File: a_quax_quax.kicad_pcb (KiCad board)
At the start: 2 copper layers, 100.3 x 94.5 mm, 23 parts

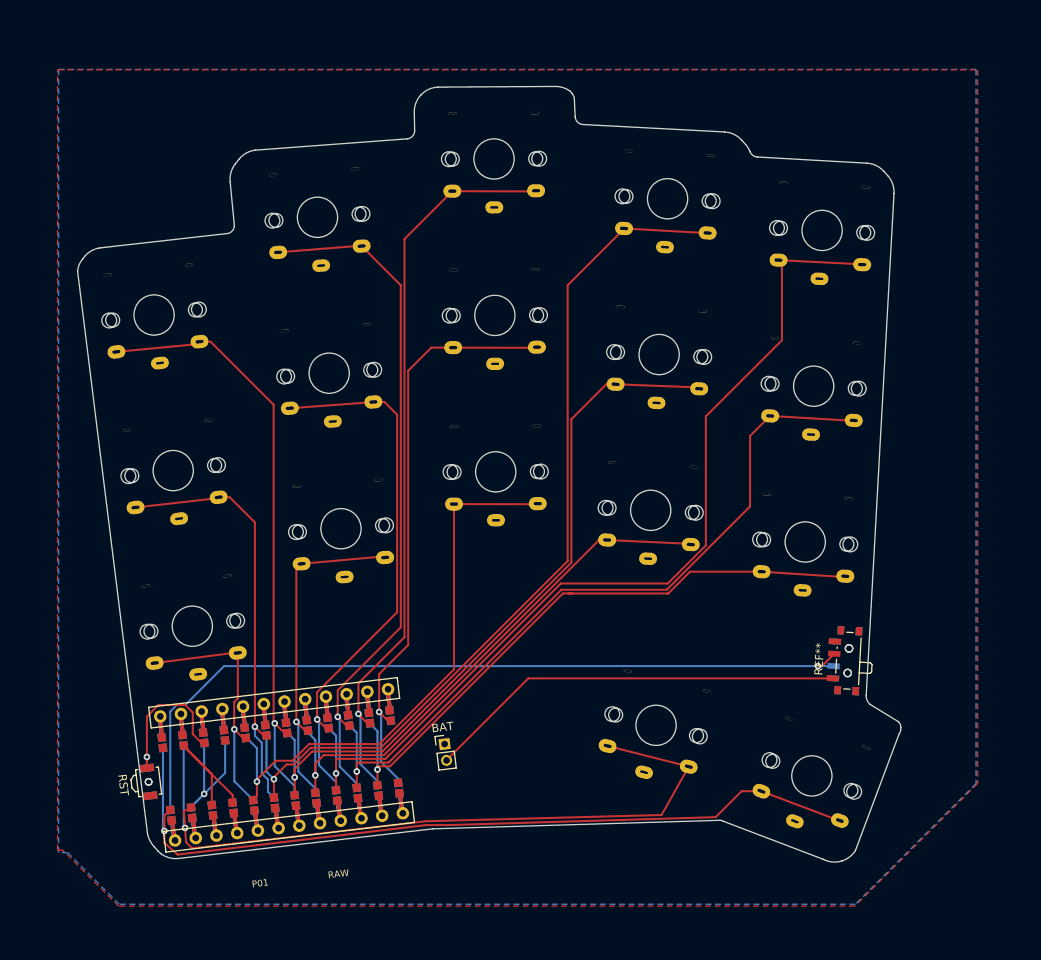
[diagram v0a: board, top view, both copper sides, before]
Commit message: update spacing and outline
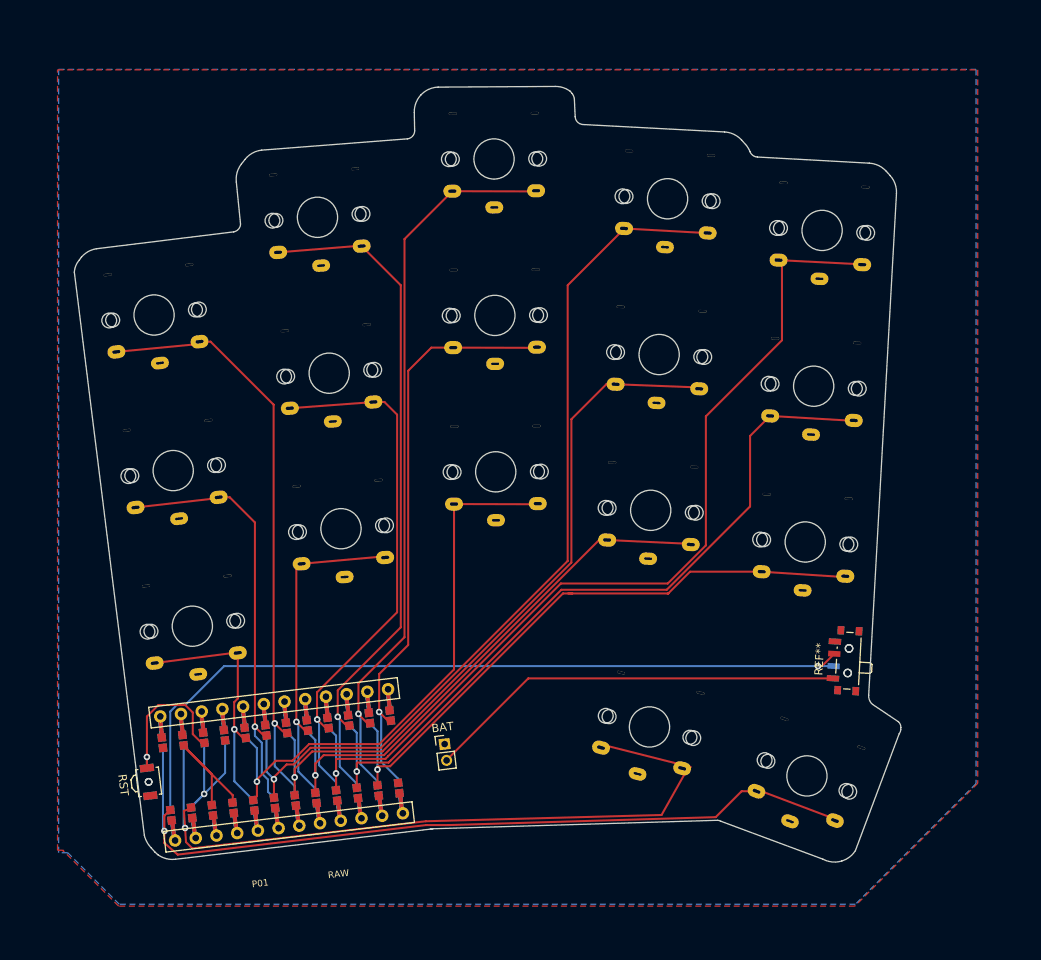
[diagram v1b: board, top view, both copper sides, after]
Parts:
- moved S32 0.82 mm to (248.0, 135.8)
- moved S34 0.60 mm to (267.1, 141.8)
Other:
- board size 100.3 x 94.5 mm -> 100.7 x 94.5 mm

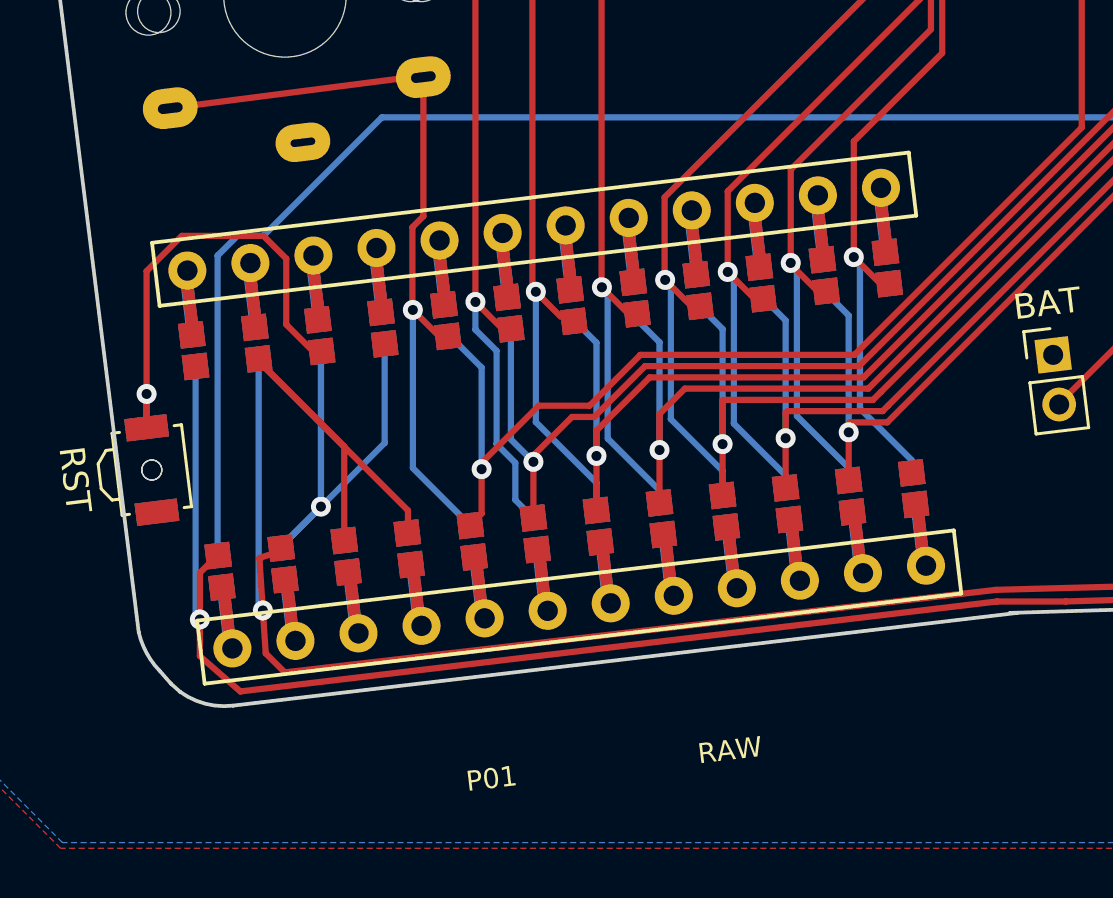
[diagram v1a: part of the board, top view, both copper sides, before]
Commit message: update ground plane
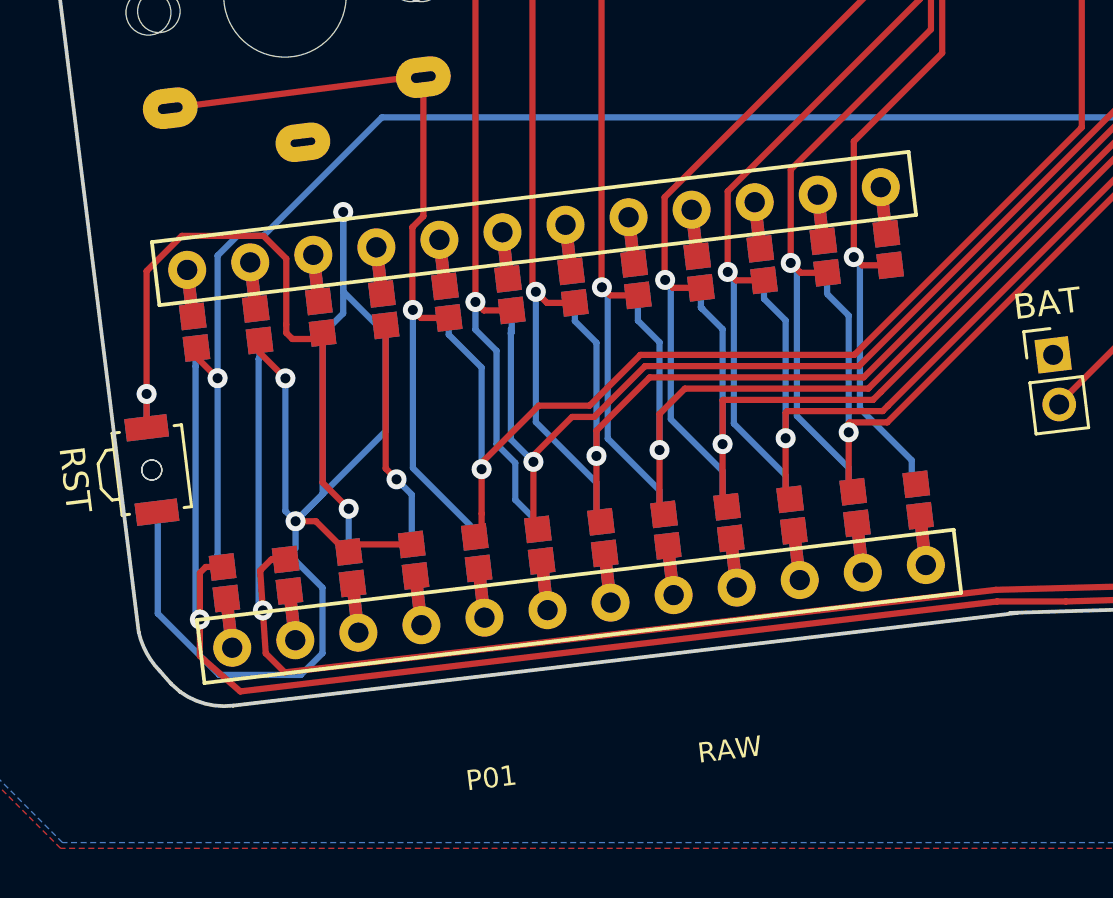
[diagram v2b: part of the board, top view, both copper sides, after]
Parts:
- C1: footprint artboard:ProMicro_Jumper -> depadiernos-parts:ProMicro_Jumper
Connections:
- C1 pad 13: P1 -> P9
- C1 pad 14: P0 -> P8
- C1 pad 15: GND -> P7
- C1 pad 16: GND -> P6
- C1 pad 17: P2 -> P5
- C1 pad 18: P3 -> P4
- C1 pad 19: P4 -> P3
- C1 pad 20: P5 -> P2
- C1 pad 21: P6 -> GND
- C1 pad 22: P7 -> GND
- C1 pad 23: P8 -> P0
- C1 pad 24: P9 -> P1
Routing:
- net GND: track 36.1 -> 58.6 mm, vias 1 -> 3
- net RST: track 18.7 -> 28.0 mm, vias 1 -> 2
- net VCC: track 0.00 -> 9.19 mm, vias 0 -> 1
- net RAW: track 97.7 -> 99.3 mm, vias 1 -> 2
- net P2: track 68.6 -> 69.6 mm
- net P3: track 108.3 -> 109.3 mm
- net P6: track 114.6 -> 115.5 mm
- net P4: track 87.7 -> 88.6 mm
- net P5: track 66.3 -> 67.1 mm
- net P0: track 90.4 -> 91.0 mm
- net P8: track 76.0 -> 76.7 mm
- net P7: track 92.1 -> 92.7 mm
- net P1: track 99.8 -> 100.5 mm

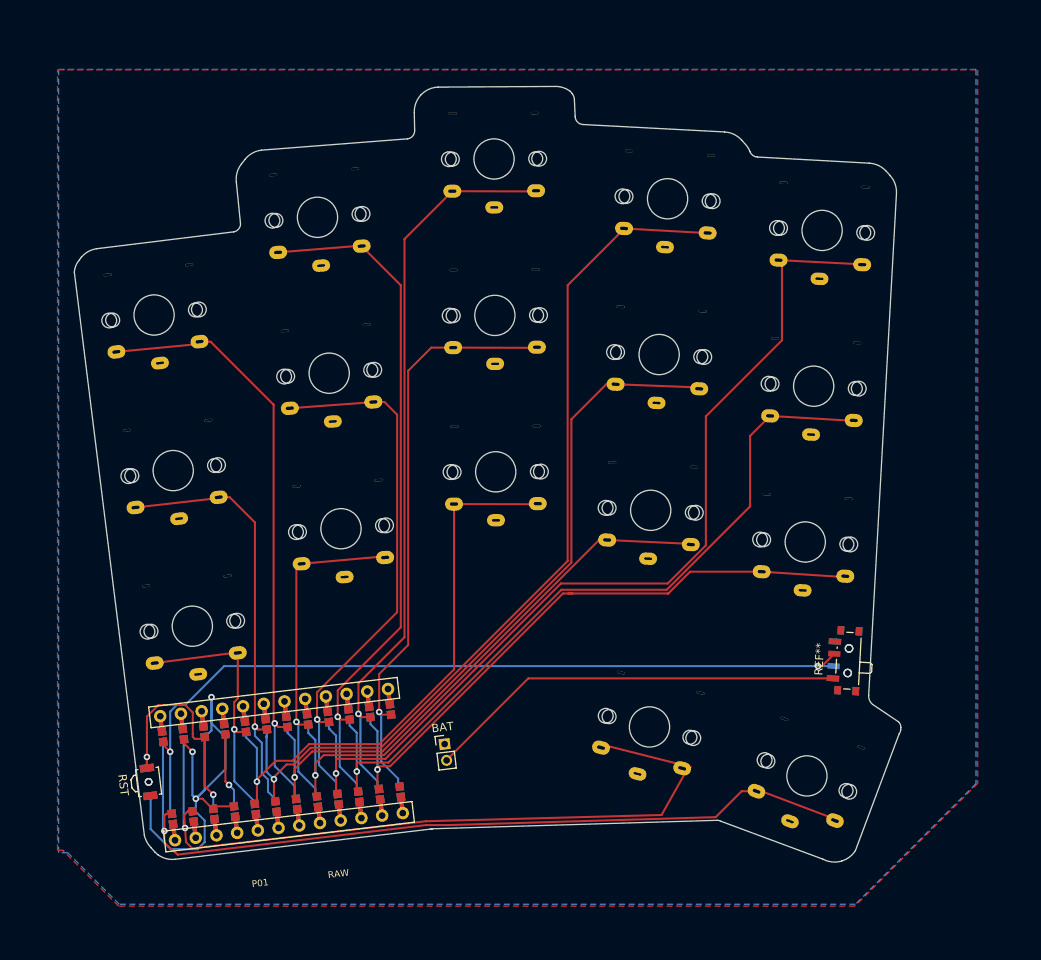
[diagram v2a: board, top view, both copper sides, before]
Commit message: fix solder mask on choc footprint
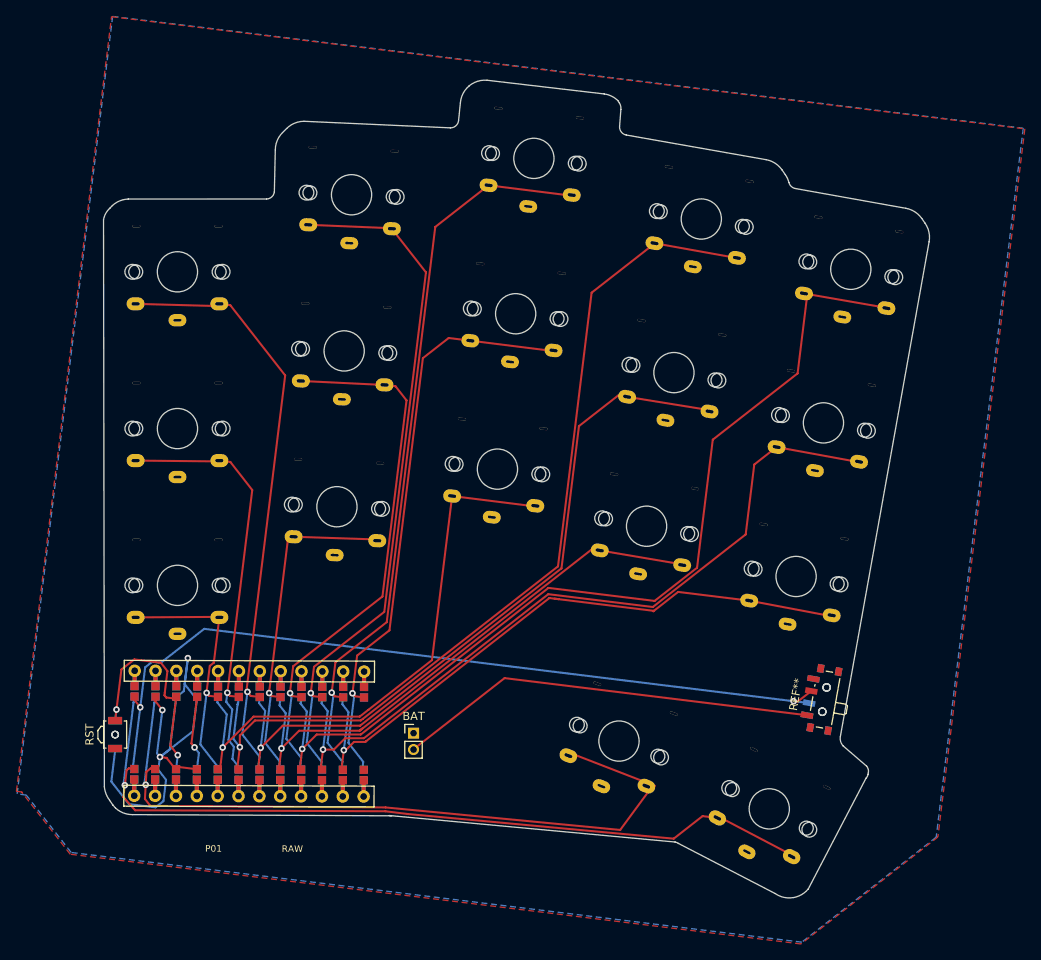
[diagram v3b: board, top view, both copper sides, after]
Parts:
- moved RST 7.06 mm to (182.9, 136.8), turned to 270 degrees
- moved RST 7.06 mm to (182.9, 136.8), turned to 90 degrees
- moved S34 6.09 mm to (262.5, 145.8), turned to 332.5 degrees
- moved S6 5.98 mm to (190.5, 80.4), turned to 0 degrees
- moved S30 5.88 mm to (272.5, 80.1), turned to 349.9 degrees
- moved REF** 5.52 mm to (268.9, 132.4), turned to 259.9 degrees
- moved REF** 5.52 mm to (268.9, 132.4), turned to 79.9 degrees
- moved C1 5.42 mm to (199.7, 136.7), turned to 89.8 degrees
- moved S2 5.29 mm to (190.5, 118.6), turned to 0 degrees
- moved S4 5.14 mm to (190.5, 99.5), turned to 0 degrees
- moved S12 4.97 mm to (211.7, 71.0), turned to 357.3 degrees
- moved S18 4.86 mm to (233.9, 66.6), turned to 353.3 degrees
- moved S24 4.79 mm to (254.3, 74.0), turned to 349.9 degrees
- moved S28 4.62 mm to (269.1, 98.8), turned to 349.9 degrees
- moved S26 4.34 mm to (265.8, 117.5), turned to 349.9 degrees
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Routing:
- net P6: track 115.5 -> 114.4 mm
- net P4: track 88.6 -> 87.8 mm
- net P7: track 92.7 -> 92.1 mm
- net P5: track 67.1 -> 66.5 mm
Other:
- board size 100.7 x 94.5 mm -> 100.6 x 99.6 mm

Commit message: fix missing via for the power switch
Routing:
- net BAT: track 51.3 -> 53.3 mm, vias 0 -> 1
